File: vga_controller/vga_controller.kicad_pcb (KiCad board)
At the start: 2 copper layers, 100 x 58 mm, 43 parts, among them J1 RJE37-188-2410, SW1 SW_Push_LED, SW2 SW_Push_LED, SW3 SW_Push_LED, SW4 SW_Push_LED, SW5 SW_Push_LED, SW6 SW_Push_LED, SW7 SW_Push_LED, SW8 SW_Push_LED, U1 NPIC6C596ADJ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

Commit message: Rev 4 of main board
controller rev1 done as well :D
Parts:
- added H1: MountingHole_Pad, MountingHole:MountingHole_3.2mm_M3_Pad, F.Cu at (150.0, 81.0)
- added H2: MountingHole_Pad, MountingHole:MountingHole_3.2mm_M3_Pad, F.Cu at (212.0, 86.0)
- added H3: MountingHole_Pad, MountingHole:MountingHole_3.2mm_M3_Pad, F.Cu at (170.0, 66.0)
- added R21: 10k, Resistor_SMD:R_0603_1608Metric_Pad0.98x0.95mm_HandSolder, B.Cu at (173.7, 74.1)
- moved R16 6.72 mm to (159.0, 66.0), turned to 180 degrees
- moved C8 6.62 mm to (159.1, 68.0), turned to 180 degrees
- moved R12 4.51 mm to (164.2, 88.0)
- moved C1 1.05 mm to (169.2, 74.1)
- moved R3 1.05 mm to (171.2, 74.1)
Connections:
- net /din renamed /copi
- net /din_pl_n renamed /ie_n
- net /dout renamed /cipo
- net /dout_shift_clk renamed /out_shift_clk
- J1 pad 5: /dout_oe_n -> GND
- U1 pad 13: /dout_oe_n -> /oe_n
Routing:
- net /dout_oe_n: track 27.0 -> 0.00 mm
- net /dout2: track 115.3 -> 90.1 mm
- net /din3: track 84.4 -> 75.5 mm
- net /din7: track 63.4 -> 57.0 mm
- net /dout6: track 52.3 -> 47.5 mm
- net /dout1: track 38.6 -> 43.4 mm
- net /clk: track 44.9 -> 40.6 mm
- net /dout7: track 16.1 -> 12.5 mm
- net Net-(R12-Pad1): track 10.2 -> 13.8 mm
- net /dout0: track 48.7 -> 45.5 mm
- net /oe_n: track 0.00 -> 2.91 mm
- net GND: track 59.2 -> 61.5 mm, vias 17 -> 18
- net /din1: track 79.4 -> 80.5 mm
- net /out_shift_clk: track 31.4 -> 30.5 mm
- net /din5: track 94.8 -> 95.6 mm
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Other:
- outline, holes or cut-outs redrawn
- board text added: "JLCJLCJLCJLC"
- board text added: "Shift Controller V1 Anton Lööf 2022"

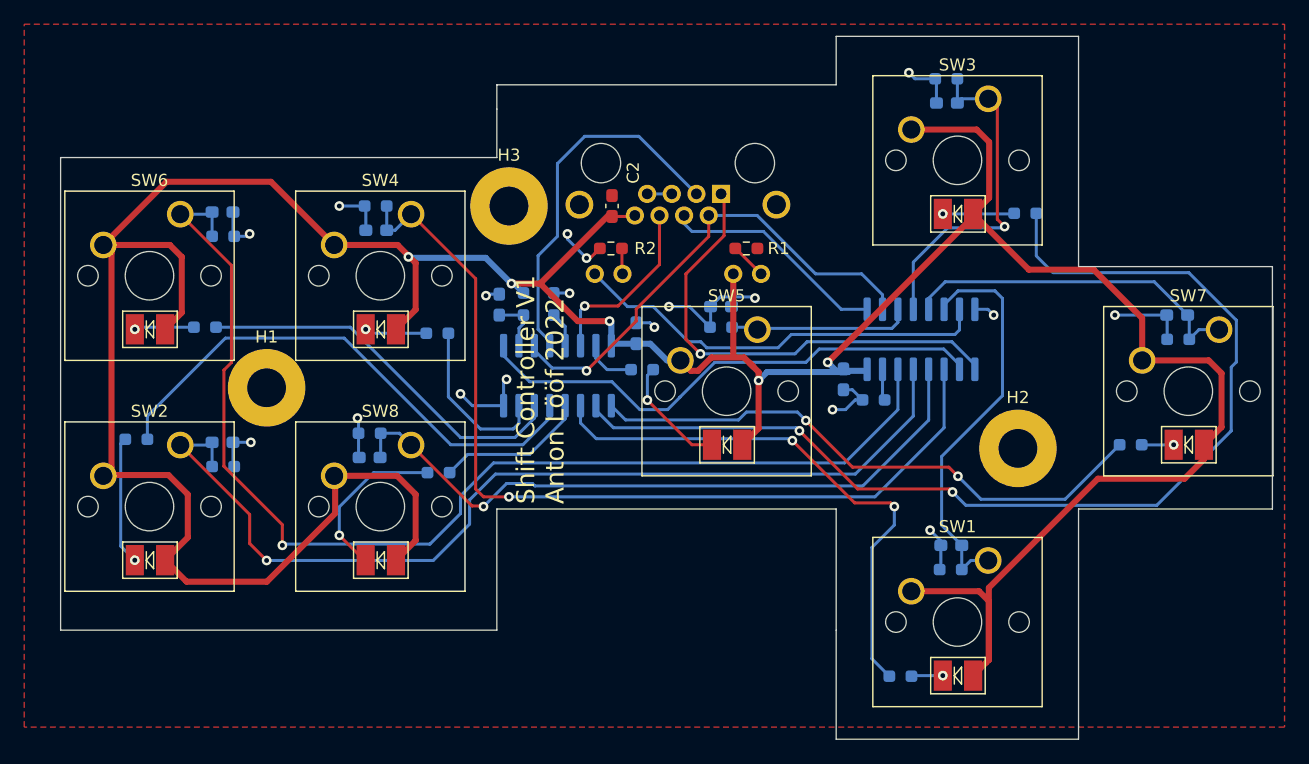
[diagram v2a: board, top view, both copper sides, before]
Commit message: fix issue with controller board
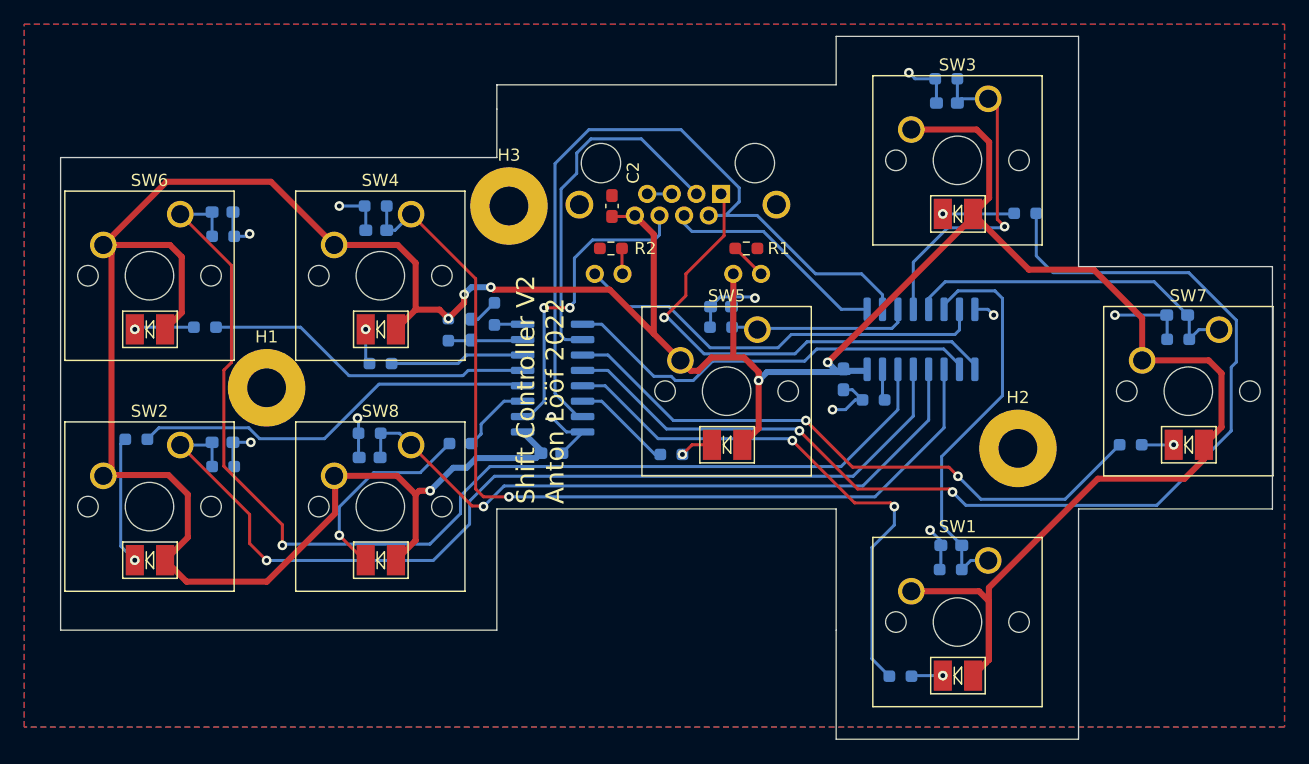
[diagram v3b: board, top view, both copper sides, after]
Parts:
- removed U1: NPIC6C596ADJ, Package_SO:SOIC-16_3.9x9.9mm_P1.27mm
- added U101: NPIC6C595, Package_SO:SOIC-16_3.9x9.9mm_P1.27mm, B.Cu at (173.6, 80.2)
- moved C4 12.1 mm to (173.5, 86.4), turned to 0 degrees
- moved R9 7.40 mm to (183.4, 86.5)
- moved R3 6.55 mm to (165.0, 76.2)
- moved R8 5.31 mm to (159.4, 79.0)
- moved R21 4.97 mm to (168.8, 74.9)
- moved C1 3.09 mm to (166.9, 76.2)
- moved R12 3.01 mm to (166.0, 85.6)
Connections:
- net /dout_clear_n renamed /dout_mr_n
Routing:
- net /clk: track 40.6 -> 62.8 mm, vias 1 -> 0
- net +3V3: track 296.6 -> 310.8 mm, vias 5 -> 6
- net /copi: track 15.1 -> 25.8 mm, vias 1 -> 2
- net GND: track 61.5 -> 51.0 mm, vias 18 -> 11
- net /dout1: track 43.4 -> 33.6 mm
- net /data_shift: track 43.3 -> 35.0 mm
- net Net-(R9-Pad1): track 9.57 -> 2.77 mm
- net /dout7: track 12.5 -> 6.14 mm
- net /dout5: track 31.7 -> 27.1 mm
- net /dout4: track 4.33 -> 8.23 mm
- net /dout6: track 47.5 -> 51.1 mm
- net Net-(R12-Pad1): track 13.8 -> 16.6 mm
- net /dout3: track 13.8 -> 11.1 mm
- net Net-(R8-Pad1): track 5.13 -> 2.95 mm
- net /dout2: track 90.1 -> 92.2 mm
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- added copper zone on B.Cu, net GND
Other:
- board text added: "Shift Controller V2 Anton Lööf 2022"
- board text removed: "Shift Controller V1 Anton Lööf 2022"
